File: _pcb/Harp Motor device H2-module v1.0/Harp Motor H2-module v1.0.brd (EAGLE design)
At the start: 58 x 52.5 mm, 82 parts, among them IC1 FT232RL, IC10 OPA365, IC11 74LVC1G125DBV, IC12 74LVC1G125DBV, IC3 LP5907MFX-3.3, IC7 USBLC6-2SC6, IC8 ATXMEGA32A4U, IC9 TLV70033DDCR, T1 DMG1012UW??, T2 DMG1012UW??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

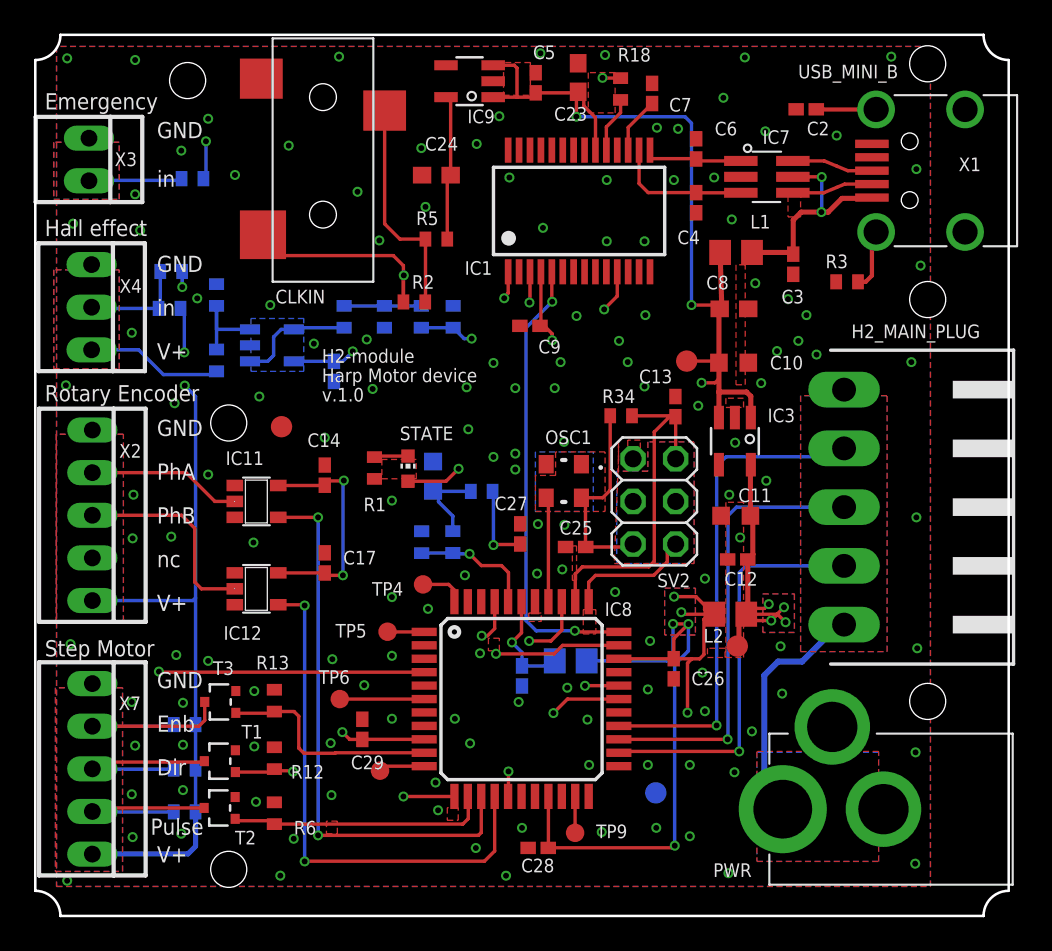
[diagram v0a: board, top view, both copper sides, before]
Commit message: Harp Motor device H2-module v1.0 - final changes
Harp Motor device H2-module v1.0 - final PCB changes
- labels sizes & positions modified
- removed clock conn from micro to main plug; added direct buffer from clock_in to main harp plug;
- corrected Harp_Tx & Harp_Rx pins
- still missing BOM & OEPS components codes
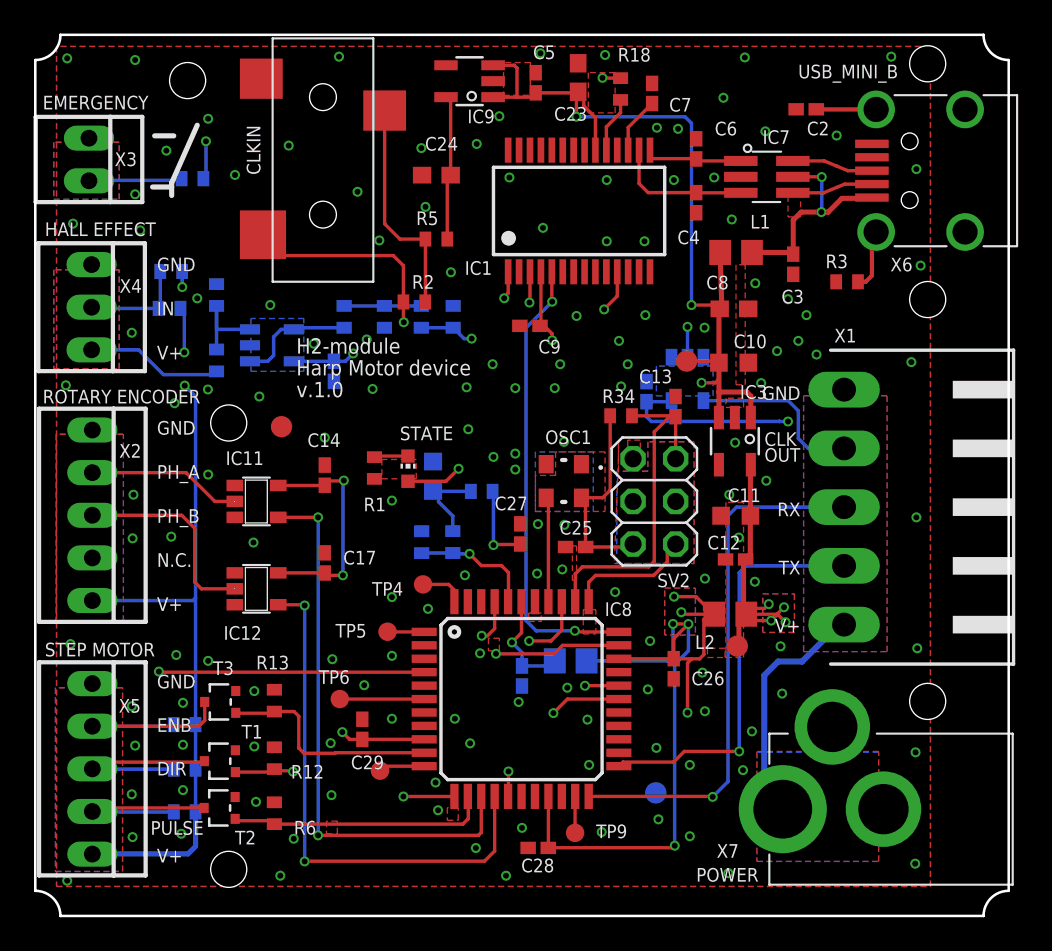
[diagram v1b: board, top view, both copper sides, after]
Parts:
- removed H2_MAIN_PLUG: be sure about plug type, Harp Motor H2-module v1.0:90G-5
- removed PWR: DC_JACK2.1MM, harp camera controller:DC_POWER_INPUT_2.1MM
- added C18: 100nF, Harp Motor H2-module v1.0:C0402K
- added IC2: 74LVC1G125DBV, Harp Motor H2-module v1.0:SOT23-5
- added X5: STEP_MOTOR, Harp Motor H2-module v1.0:22-23-2051
- added X6: USB_MINI_B, VestibularVR H1-module v1.0:240-0002-1
- X1: value USB_MINI_B -> be sure about plug type; device VestibularVR H1-module v1.0:240-0002-1 -> Harp Motor H2-module v1.0:90G-5
- X7: value STEP_MOTOR -> DC_JACK2.1MM; device Harp Motor H2-module v1.0:22-23-2051 -> harp camera controller:DC_POWER_INPUT_2.1MM
- moved X7 49.7 mm to (53.0, 6.36), turned to 180 degrees
- moved X1 20.7 mm to (53.4, 24.4)
- moved C12 0.13 mm to (41.7, 21.2)
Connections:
- removed net CLOCK_IN: CLKIN.4, IC8.12, R2.1
- removed net HARP_H2_CLOCK_IN: H2_MAIN_PLUG.4, IC8.26
- new net HARP_H2_CLOCK_OUT: IC2.4, X1.4
- new net U_CLOCK_IN: CLKIN.4, IC2.2, IC8.12, R2.1
- net +3V3: now also C18.1, IC2.5
- net +5V: now also X5.5; no longer X7.5
- net GND: now also C18.2, IC2.1, IC2.3, X1.5, X5.1, X6.P$5, X7.P2, X7.P3; no longer H2_MAIN_PLUG.5, PWR.P2, PWR.P3, X1.P$5, X7.1
- net HARP_H2_RX: now also IC8.22, X1.3; no longer H2_MAIN_PLUG.3, IC8.25
- net HARP_H2_TX: now also IC8.23, X1.2; no longer H2_MAIN_PLUG.2, IC8.24
- net N$1: now also X6.SHIELD_4; no longer X1.SHIELD_4
- net N$15: now also X6.SHIELD_3; no longer X1.SHIELD_3
- net N$2: now also X6.P$2; no longer X1.P$2
- net N$3: now also X6.P$3; no longer X1.P$3
- net STEP_DIRECTION: now also X5.3; no longer X7.3
- net STEP_ENABLE: now also X5.2; no longer X7.2
- net STEP_PULSE: now also X5.4; no longer X7.4
- net USB_POWER: now also X6.P$1; no longer X1.P$1
- net VDD: now also X1.1, X7.P1; no longer H2_MAIN_PLUG.1, PWR.P1
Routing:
- net U_CLOCK_IN: track 0.00 -> 62.9 mm, vias 0 -> 3
- net CLOCK_IN: track 47.2 -> 0.00 mm, vias 2 -> 0
- net HARP_H2_CLOCK_IN: track 29.3 -> 0.00 mm, vias 1 -> 0
- net +3V3: track 219.8 -> 230.7 mm, vias 15 -> 16
- net HARP_H2_CLOCK_OUT: track 0.00 -> 10.5 mm
- net HARP_H2_RX: track 26.9 -> 31.7 mm
- added copper zone on layer 16, net N$66
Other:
- board text added: "CLK OUT"
- board text added: "EMERGENCY"
- board text added: "GND ENB DIR V+"
- board text added: "GND IN V+"
- board text added: "GND PH_A PH_B N.C. V+"
- board text added: "GND RX TX V+"
- board text added: "HALL EFFECT"
- board text added: "POWER"
- board text added: "PULSE"
- board text added: "ROTARY ENCODER"
- board text added: "STEP MOTOR"
- board text removed: "Emergency"
- board text removed: "GND Enb Dir V+"
- board text removed: "GND PhA PhB nc V+"
- board text removed: "GND in"
- board text removed: "GND in V+"
- board text removed: "Hall effect"
- board text removed: "Pulse"
- board text removed: "Rotary Encoder"
- board text removed: "Step Motor"

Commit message: Harp Motor device H2-module v1.0 - BOM not finished
Harp Motor device H2-module v1.0
- BOM committed; not yet finished
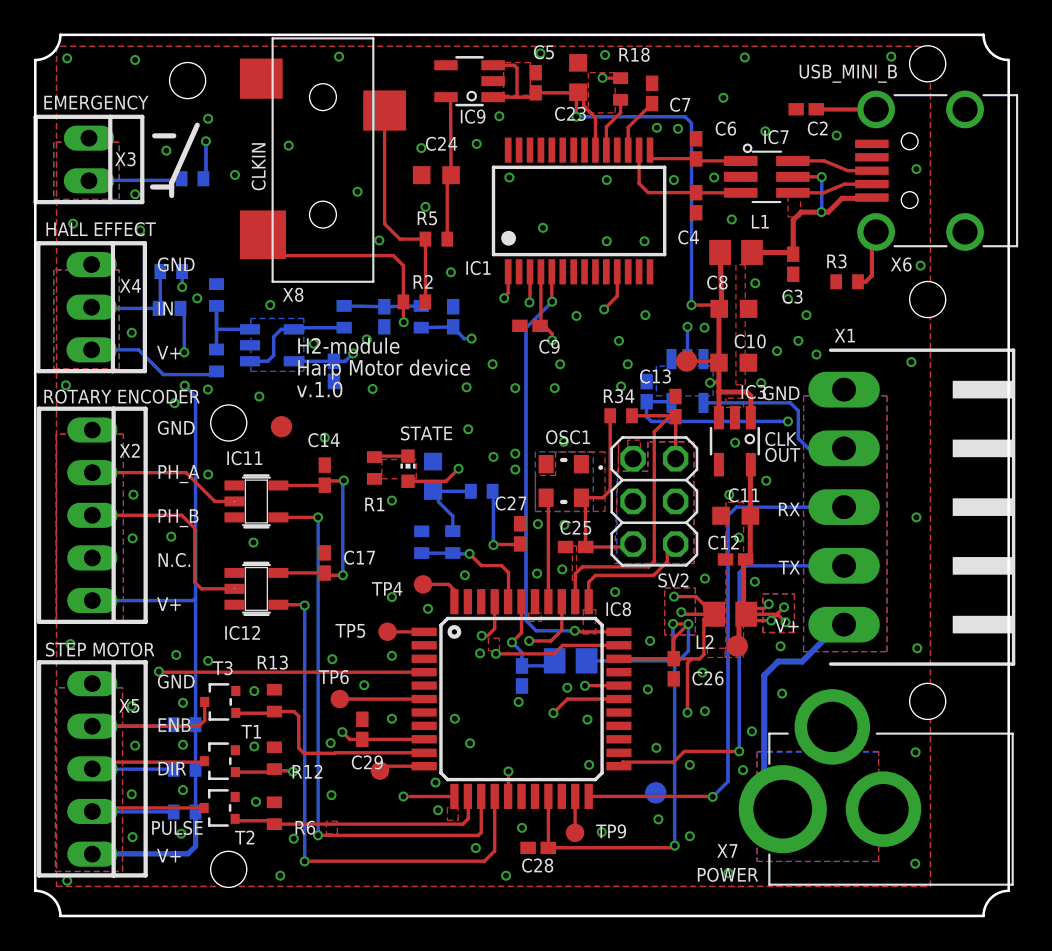
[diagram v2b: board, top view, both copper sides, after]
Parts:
- removed CLKIN: CLCK_JACK, harp input expander:35RASMT2BHNTRX
- added X8: CLCK_JACK, Harp Motor H2-module v1.0:35RASMT2BHNTRX
- C15: value 4.7uF DNI -> 4.7uF
- C23, C24: device rcl:C0603 -> Harp Motor H2-module v1.0:C0603K
- C41, C42: device rcl:C0402 -> Harp Motor H2-module v1.0:C0402K
- C8: device Harp Motor H2-module v1.0:C0603 -> Harp Motor H2-module v1.0:C0603K
- IC1: device VestibularVR H1-module v1.0:SSOP28 -> Harp Motor H2-module v1.0:SSOP28
- IC10: device CNP-ics 2:SOT23-5 -> Harp Motor H2-module v1.0:SOT23-5
- IC3: device VestibularVR H1-module v1.0:TSOT23-5 -> Harp Motor H2-module v1.0:TSOT23-5
- IC7: device VestibularVR H1-module v1.0:SOT23-6L -> Harp Motor H2-module v1.0:SOT23-6L
- IC8: device VestibularVR H1-module v1.0:TQFP44 -> Harp Motor H2-module v1.0:TQFP44
- IC9: value TLV70033DDCR -> LP5907MFX-3.3; device harp input expander:TSOT23-5 -> Harp Motor H2-module v1.0:TSOT23-5
- OSC1: device VestibularVR H1-module v1.0:OSCILLATOR_3.2X2.5 -> Harp Motor H2-module v1.0:OSCILLATOR_3.2X2.5
- R1, R11, R12, R14, R15, R16, R18, R2, R3, R34, R5, R6, R8: device Harp Motor H2-module v1.0:R0402$1 -> Harp Motor H2-module v1.0:R0402
- R10: value DNI -> DNI 0R; device Harp Motor H2-module v1.0:R0402$1 -> Harp Motor H2-module v1.0:R0402
- R13: value DNI -> 10k; device Harp Motor H2-module v1.0:R0402$1 -> Harp Motor H2-module v1.0:R0402
- R17, R19: value 10k 1% -> 10k; device rcl:R0402 -> Harp Motor H2-module v1.0:R0402
- R20, R21: device rcl:R0402 -> Harp Motor H2-module v1.0:R0402
- R4: value 0R DNI -> div tensao ADC; device Harp Motor H2-module v1.0:R0402$1 -> Harp Motor H2-module v1.0:R0402
- R7: value 10k DNI -> div tensao ADC; device Harp Motor H2-module v1.0:R0402$1 -> Harp Motor H2-module v1.0:R0402
- R9: value 100R DNI -> DNI 100R; device Harp Motor H2-module v1.0:R0402$1 -> Harp Motor H2-module v1.0:R0402
- T1, T2, T3: value DMG1012UW?? -> DMG1012UW; device VestibularVR H1-module v1.0:SOT323 -> Harp Motor H2-module v1.0:SOT323
- X1: value be sure about plug type -> 1x5 MAIN PLUG
- X2: value Rot_Encoder -> 1x5 case
- X3: value EMRG_BUTT_IN_NO -> 1x2 case
- X4: value Hall_Effect -> 1x3 case
- X5: value STEP_MOTOR -> 1x5 case
- X6: device VestibularVR H1-module v1.0:240-0002-1 -> Harp Motor H2-module v1.0:240-0002-1
- X7: device harp camera controller:DC_POWER_INPUT_2.1MM -> Harp Motor H2-module v1.0:DC_POWER_INPUT_2.1MM
- moved IC2 0.13 mm to (38.9, 31.9)
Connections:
- net +3V3_U renamed V+
- net GND: now also X8.5; no longer CLKIN.5
- net N$103: now also X8.1; no longer CLKIN.1
- net U_CLOCK_IN: now also X8.4; no longer CLKIN.4
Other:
- board text added: "CLKIN"

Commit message: Harp Motor device H2-module v1.0 - BOM updated
Harp Motor device H2-module v1.0 - BOM updated
- still missing component's codes
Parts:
- C15: value 4.7uF -> DNI 4.7uF
- R4, R7: value div tensao ADC -> DNI
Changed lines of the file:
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@@
 </element>
 <element name="R5" library="Harp Motor H2-module v1.0" package="R0402" value="10R" x="23.898" y="40.33" smashed="yes" rot="R180">
-<attribute name="MPN" value="ERJ-PA2J100X
-" x="23.898" y="40.33" size="1.778" layer="27" rot="R180" display="off"/>
+<attribute name="MPN" value="ERJ-PA2J100X " x="23.898" y="40.33" size="1.778" layer="27" rot="R180" display="off"/>
 <attribute name="NAME" x="24.025" y="41.981" size="0.8128" layer="25" font="vector" ratio="15" rot="R180"/>
-<attribute name="OEPS" value="OEPS020041
-" x="23.898" y="40.33" size="1.778" layer="27" rot="R180" display="off"/>
+<attribute name="OEPS" value="OEPS020041 " x="23.898" y="40.33" size="1.778" layer="27" rot="R180" display="off"/>
 <attribute name="VALUE" x="24.533" y="42.235" size="1.27" layer="27" rot="R180"/>
 </element>
@@
 <attribute name="VALUE" x="47.038" y="1.614" size="0.6096" layer="27" rot="R180"/>
 </element>
-<element name="R4" library="Harp Motor H2-module v1.0" package="R0402" value="div tensao ADC" x="24.8772" y="22.2772" smashed="yes" rot="MR90">
-<attribute name="MPN" value="n.a" x="24.8772" y="22.2772" size="1.778" layer="28" rot="MR90" display="off"/>
+<element name="R4" library="Harp Motor H2-module v1.0" package="R0402" value="DNI" x="24.8772" y="22.2772" smashed="yes" rot="MR90">
+<attribute name="MPN" value="DNI" x="24.8772" y="22.2772" size="1.778" layer="28" rot="MR90" display="off"/>
 <attribute name="NAME" x="24.4646" y="20.5478" size="0.8128" layer="26" font="vector" ratio="15" rot="MR180"/>
-<attribute name="OEPS" value="TBD" x="24.8772" y="22.2772" size="1.778" layer="28" rot="MR90" display="off"/>
+<attribute name="OEPS" value="DNI" x="24.8772" y="22.2772" size="1.778" layer="28" rot="MR90" display="off"/>
 <attribute name="VALUE" x="22.9722" y="21.6422" size="1.27" layer="28" rot="MR90"/>
 </element>
-<element name="R7" library="Harp Motor H2-module v1.0" package="R0402" value="div tensao ADC" x="23.024" y="22.272" smashed="yes" rot="MR270">
-<attribute name="MPN" value="n.a." x="23.024" y="22.272" size="1.778" layer="28" rot="MR270" display="off"/>
+<element name="R7" library="Harp Motor H2-module v1.0" package="R0402" value="DNI" x="23.024" y="22.272" smashed="yes" rot="MR270">
+<attribute name="MPN" value="DNI" x="23.024" y="22.272" size="1.778" layer="28" rot="MR270" display="off"/>
 <attribute name="NAME" x="22.0622" y="20.4966" size="0.8128" layer="26" font="vector" ratio="15" rot="MR180"/>
-<attribute name="OEPS" value="TBD" x="23.024" y="22.272" size="1.778" layer="28" rot="MR270" display="off"/>
+<attribute name="OEPS" value="DNI" x="23.024" y="22.272" size="1.778" layer="28" rot="MR270" display="off"/>
 <attribute name="VALUE" x="24.929" y="22.907" size="1.27" layer="28" rot="MR270"/>
 </element>
@@
 <attribute name="VALUE" x="29.976" y="36.612" size="1.016" layer="27" rot="R180"/>
 </element>
-<element name="C15" library="Harp Motor H2-module v1.0" package="C0603K" value="4.7uF" x="23.7" y="26.2" smashed="yes" rot="MR90">
+<element name="C15" library="Harp Motor H2-module v1.0" package="C0603K" value="DNI 4.7uF" x="23.7" y="26.2" smashed="yes" rot="MR90">
 <attribute name="MPN" value="C1608X6S1C475K080AC" x="23.7" y="26.2" size="1.778" layer="28" rot="MR90" display="off"/>
 <attribute name="NAME" x="24.4" y="27.95" size="0.8128" layer="26" font="vector" ratio="15" rot="MR0"/>
@@
 </element>
 <element name="R9" library="Harp Motor H2-module v1.0" package="R0402" value="DNI 100R" x="26.6" y="25.3" smashed="yes" rot="MR180">
-<attribute name="MPN" value="ERJ-2RKF1000X
-" x="26.6" y="25.3" size="1.778" layer="28" rot="MR180" display="off"/>
+<attribute name="MPN" value="ERJ-2RKF1000X " x="26.6" y="25.3" size="1.778" layer="28" rot="MR180" display="off"/>
 <attribute name="NAME" x="26.565" y="24.465" size="0.8128" layer="26" font="vector" ratio="15" rot="MR180"/>
 <attribute name="OEPS" value="OEPS020004" x="26.6" y="25.3" size="1.778" layer="28" rot="MR180" display="off"/>

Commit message: Harp Motor device H2-module v1.0 BOM updated
Harp Motor device H2-module v1.0 BOM updated
- OEPS & MPN components code changed
- new BOM generated
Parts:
- IC10: value OPA365 -> THS4281DBVT
- IC11, IC12, IC2: value 74LVC1G125DBV -> SN74LVC1G125DBVT
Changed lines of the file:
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@@
 <attribute name="MPN" value="04025A470JAT2A" x="52.38" y="42.499" size="1.778" layer="27" rot="R270" display="off"/>
 <attribute name="NAME" x="39.5992" y="40.8378" size="0.8128" layer="25" font="vector" ratio="15" rot="R180"/>
-<attribute name="OEPS" value="OEPS080013" x="39.38" y="42.499" size="1.778" layer="27" rot="R270" display="off"/>
+<attribute name="OEPS" value="OEPS010011" x="39.38" y="42.499" size="1.778" layer="27" rot="R270" display="off"/>
 <attribute name="VALUE" x="37.475" y="43.134" size="1.27" layer="27" rot="R270"/>
 </element>
@@
 <attribute name="MPN" value="04025A470JAT2A" x="31.38" y="40.206" size="1.778" layer="27" rot="R90" display="off"/>
 <attribute name="NAME" x="40.4842" y="46.5074" size="0.8128" layer="25" font="vector" ratio="15"/>
-<attribute name="OEPS" value="OEPS080013" x="39.38" y="45.706" size="1.778" layer="27" rot="R90" display="off"/>
+<attribute name="OEPS" value="OEPS010011" x="39.38" y="45.706" size="1.778" layer="27" rot="R90" display="off"/>
 <attribute name="VALUE" x="41.285" y="45.071" size="1.27" layer="27" rot="R90"/>
 </element>
@@
 <attribute name="MPN" value="04025A470JAT2A" x="38.1448" y="30.34885" size="1.778" layer="27" rot="R90" display="off"/>
 <attribute name="NAME" x="37.95315" y="32.5526" size="0.8128" layer="25" font="vector" ratio="15" rot="R180"/>
-<attribute name="OEPS" value="OEPS080013" x="38.1448" y="30.34885" size="1.778" layer="27" rot="R90" display="off"/>
+<attribute name="OEPS" value="OEPS010011" x="38.1448" y="30.34885" size="1.778" layer="27" rot="R90" display="off"/>
 <attribute name="VALUE" x="40.0498" y="29.71385" size="1.27" layer="27" rot="R90"/>
 </element>
@@
 <attribute name="VALUE" x="24.929" y="22.907" size="1.27" layer="28" rot="MR270"/>
 </element>
-<element name="IC11" library="Harp Motor H2-module v1.0" package="SOT23-5" value="74LVC1G125DBV" x="13.178" y="24.7" smashed="yes" rot="R270">
+<element name="IC11" library="Harp Motor H2-module v1.0" package="SOT23-5" value="SN74LVC1G125DBVT" x="13.178" y="24.7" smashed="yes" rot="R270">
 <attribute name="MPN" value="SN74LVC1G125DBVT" x="13.178" y="24.7" size="1.778" layer="27" rot="R270" display="off"/>
 <attribute name="NAME" x="11.344" y="26.87" size="0.8128" layer="25" font="vector" ratio="15"/>
@@
 <attribute name="VALUE" x="9.368" y="27.24" size="1.27" layer="27" rot="R270"/>
 </element>
-<element name="IC12" library="Harp Motor H2-module v1.0" package="SOT23-5" value="74LVC1G125DBV" x="13.178" y="19.492" smashed="yes" rot="R270">
+<element name="IC12" library="Harp Motor H2-module v1.0" package="SOT23-5" value="SN74LVC1G125DBVT" x="13.178" y="19.492" smashed="yes" rot="R270">
 <attribute name="MPN" value="SN74LVC1G125DBVT" x="13.178" y="19.492" size="1.778" layer="27" rot="R270" display="off"/>
 <attribute name="NAME" x="11.218" y="16.456" size="0.8128" layer="25" font="vector" ratio="15"/>
@@
 <attribute name="VALUE" x="12.705" y="37.635" size="1.27" layer="28" rot="MR270"/>
 </element>
-<element name="IC10" library="Harp Motor H2-module v1.0" package="SOT23-5" value="OPA365" x="14.1" y="34" smashed="yes" rot="MR90">
-<attribute name="MPN" value="OEPS080019=TLV272CDGKR" x="14.1" y="34" size="1.778" layer="28" rot="MR90" display="off"/>
+<element name="IC10" library="Harp Motor H2-module v1.0" package="SOT23-5" value="THS4281DBVT" x="14.1" y="34" smashed="yes" rot="MR90">
+<attribute name="MPN" value="THS4281DBVT" x="14.1" y="34" size="1.778" layer="28" rot="MR90" display="off"/>
 <attribute name="NAME" x="12.622" y="31.922" size="0.8128" layer="26" font="vector" ratio="15" rot="MR180"/>
-<attribute name="OEPS" value="TBD" x="14.1" y="34" size="1.778" layer="28" rot="MR90" display="off"/>
+<attribute name="OEPS" value="OEPS F01 068" x="14.1" y="34" size="1.778" layer="28" rot="MR90" display="off"/>
 <attribute name="VALUE" x="12.322" y="37.048" size="1.27" layer="28" ratio="10" rot="MR180"/>
 </element>
@@
 <attribute name="VALUE" x="34.9736" y="30.742" size="1.016" layer="28" rot="MR90"/>
 </element>
-<element name="IC2" library="Harp Motor H2-module v1.0" package="SOT23-5" value="74LVC1G125DBV" x="38.862" y="31.877" smashed="yes" rot="MR180">
+<element name="IC2" library="Harp Motor H2-module v1.0" package="SOT23-5" value="SN74LVC1G125DBVT" x="38.862" y="31.877" smashed="yes" rot="MR180">
 <attribute name="MPN" value="SN74LVC1G125DBVT" x="38.862" y="31.877" size="1.778" layer="28" rot="MR180" display="off"/>
 <attribute name="NAME" x="36.068" y="35.052" size="0.8128" layer="26" font="vector" ratio="15" rot="MR180"/>
